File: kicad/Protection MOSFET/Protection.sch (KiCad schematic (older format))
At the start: 60 parts, among them P1 VI2, P2 LED, P3 VO2, P4 VI1, P5 VAC2, P6 VO1, P7 Taster, Q1 BC858, Q2 Q_NMOS_GDS, Q3 BC850, Q4 BC850, Q5 BC850, Q6 BC858, Q7 BC850, Q8 Q_NMOS_GDS, Q9 BC850, U1 LM319, U2 LTV-817

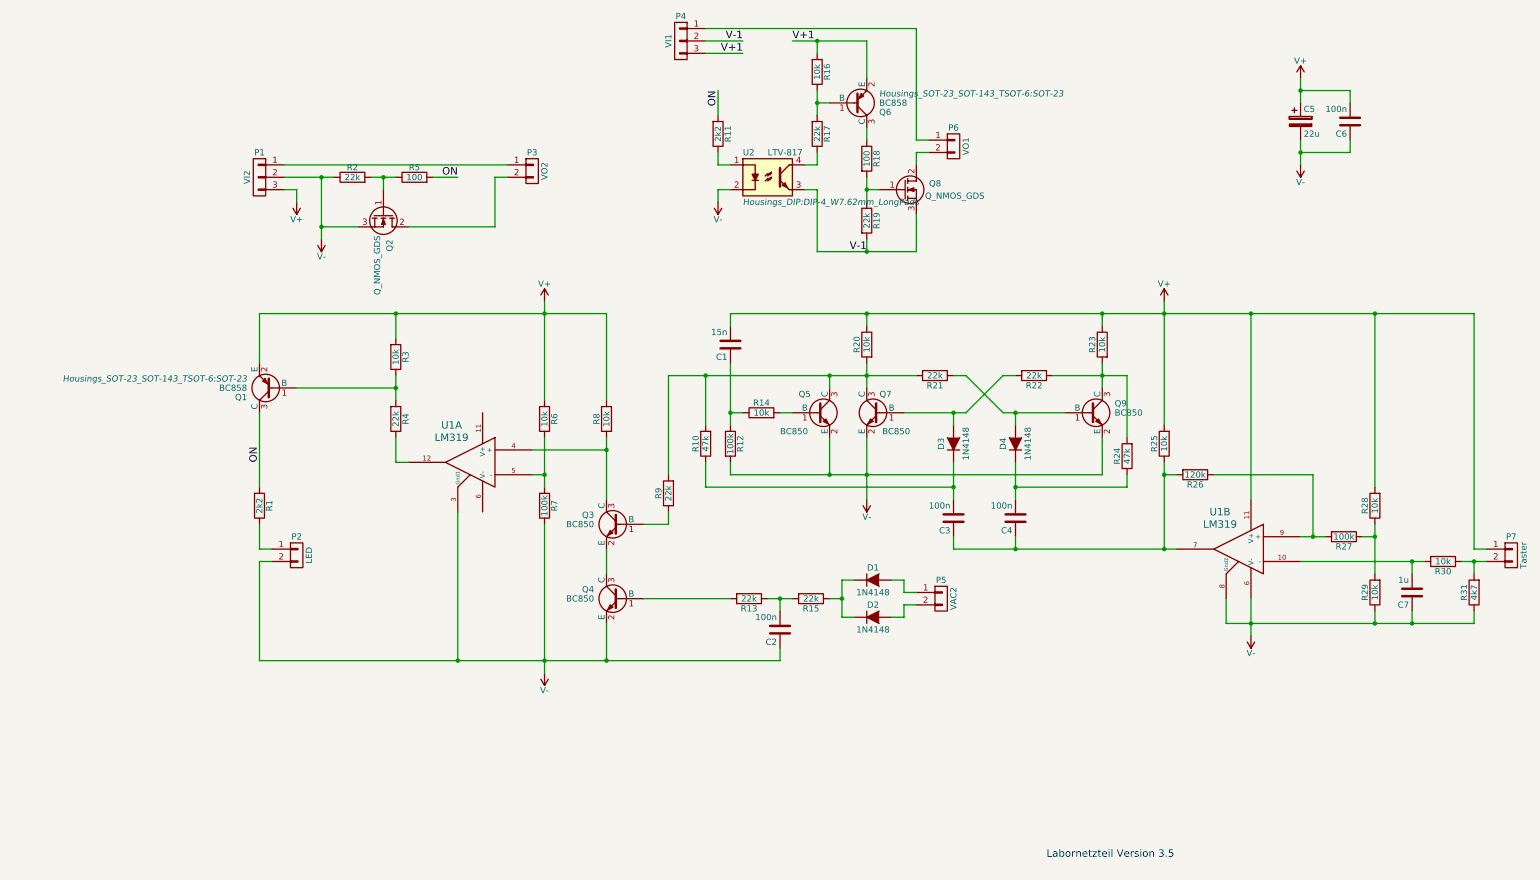
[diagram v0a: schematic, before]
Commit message: Corrected MOSFET Protection board
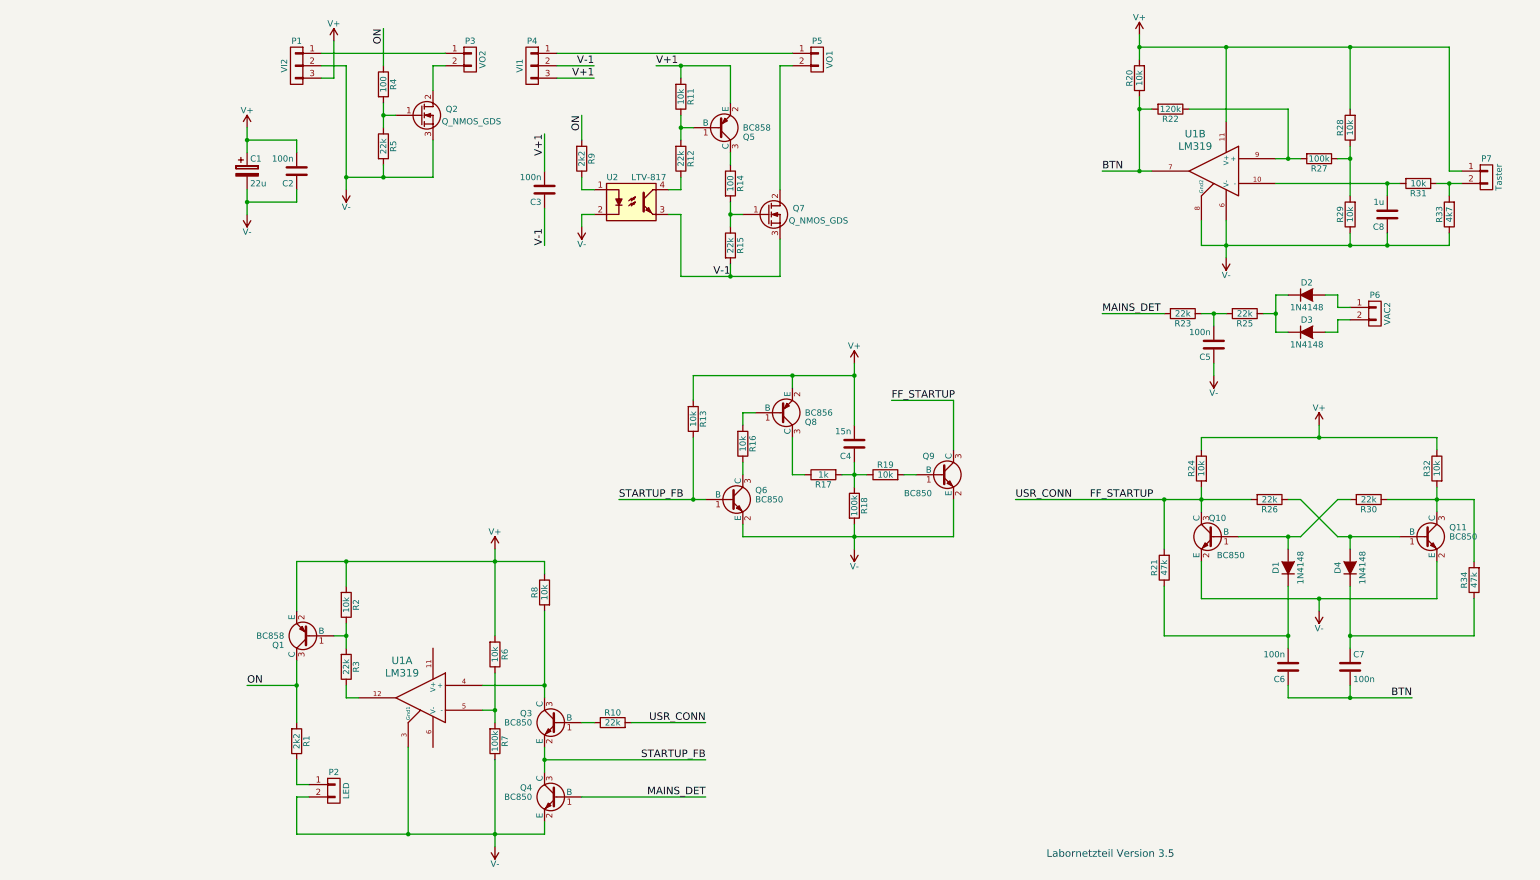
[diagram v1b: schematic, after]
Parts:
- added C3: 100n, Capacitors_SMD:C_0805, symbol C
- added Q6: BC850, TO_SOT_Packages_SMD:SOT-23, symbol BC850
- added Q8: BC856, TO_SOT_Packages_SMD:SOT-23, symbol BC856
- added R13, R16: 10k, Resistors_SMD:R_0805, symbol R
- added R17: 1k, Resistors_SMD:R_0805, symbol R
- C1: renamed from C5; footprint Capacitors_Elko_ThroughHole:Elko_vert_11.2x7.5mm_RM2.5_CopperClear -> Capacitors_ThroughHole:C_Radial_D7.5_L11.2_P2.5
- Q1, Q3, Q4: footprint Housings_SOT-23_SOT-143_TSOT-6:SOT-23 -> TO_SOT_Packages_SMD:SOT-23
- Q10: renamed from Q7; footprint Housings_SOT-23_SOT-143_TSOT-6:SOT-23 -> TO_SOT_Packages_SMD:SOT-23
- Q11: renamed from Q9; footprint Housings_SOT-23_SOT-143_TSOT-6:SOT-23 -> TO_SOT_Packages_SMD:SOT-23
- Q2: footprint Transistors_SMD:sot428 -> TO_SOT_Packages_SMD:SOT-428
- Q5: renamed from Q6; footprint Housings_SOT-23_SOT-143_TSOT-6:SOT-23 -> TO_SOT_Packages_SMD:SOT-23
- Q7: renamed from Q8; footprint Transistors_SMD:sot428 -> TO_SOT_Packages_SMD:SOT-428
- Q9: renamed from Q5; footprint Housings_SOT-23_SOT-143_TSOT-6:SOT-23 -> TO_SOT_Packages_SMD:SOT-23
- renumbered C6 to C2, C1 to C4, C2 to C5, C3 to C6, C4 to C7, C7 to C8, D3 to D1, D1 to D2, D2 to D3, P6 to P5, P5 to P6, R9 to R10, R16 to R11, R17 to R12, R18 to R14, R19 to R15, R12 to R18, R14 to R19, R3 to R2, R25 to R20, R10 to R21, R26 to R22, R13 to R23, R20 to R24, R15 to R25, R21 to R26, R4 to R3, R22 to R30, R30 to R31, R23 to R32, R31 to R33, R24 to R34, R5 to R4, R2 to R5, R11 to R9
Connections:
- net ON: now also R4.1; no longer R4.2
- net V+: now also Q8.2 (E), R13.2
- net V+1: now also C3.2
- net V-: now also R5.2, Q6.2 (E); no longer R5.1
- net V-1: now also C3.1
- net STARTUP_FB: now reaches Q3.2 (E), Q4.3 (C)
- net STARTUP_FB: now also Q6.1 (B), R13.1
- net MAINS_DET: now reaches Q4.1 (B), R23.2
- net FF_STARTUP: now reaches Q10.3 (C), Q9.3 (C), R10.2, R21.2, R24.2, R26.2
- net at D4.1 (K), R34.1: now also C7.1; no longer C7.2
- net BTN: now reaches C6.1, R20.1, R22.2, U1.7
- net BTN: now also C7.2; no longer C7.1
- net at C4.1, R18.1, R19.1: now also R17.2
- new net: Q2.1 (G), R4.2, R5.1
- new net: Q6.3 (C), R16.1
- new net: Q8.1 (B), R16.2
- new net: Q8.3 (C), R17.1
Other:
- moved on the sheet: C1, C2, C4, C5, C6, C7, C8, D1, D2, D3, D4, P1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
